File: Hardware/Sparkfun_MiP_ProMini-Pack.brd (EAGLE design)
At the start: 41.4 x 63.8 mm, 45 parts, among them Q1 8MHz, U1 ATMEGA328, U2 MIC5205, U3 TS3USB221A

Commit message: renamed files
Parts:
- added FID1, FID2: FIDUCIAL1X2, SparkFun-Aesthetics:FIDUCIAL-1X2
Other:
- board text added: "v10"
- board text removed: "v01"

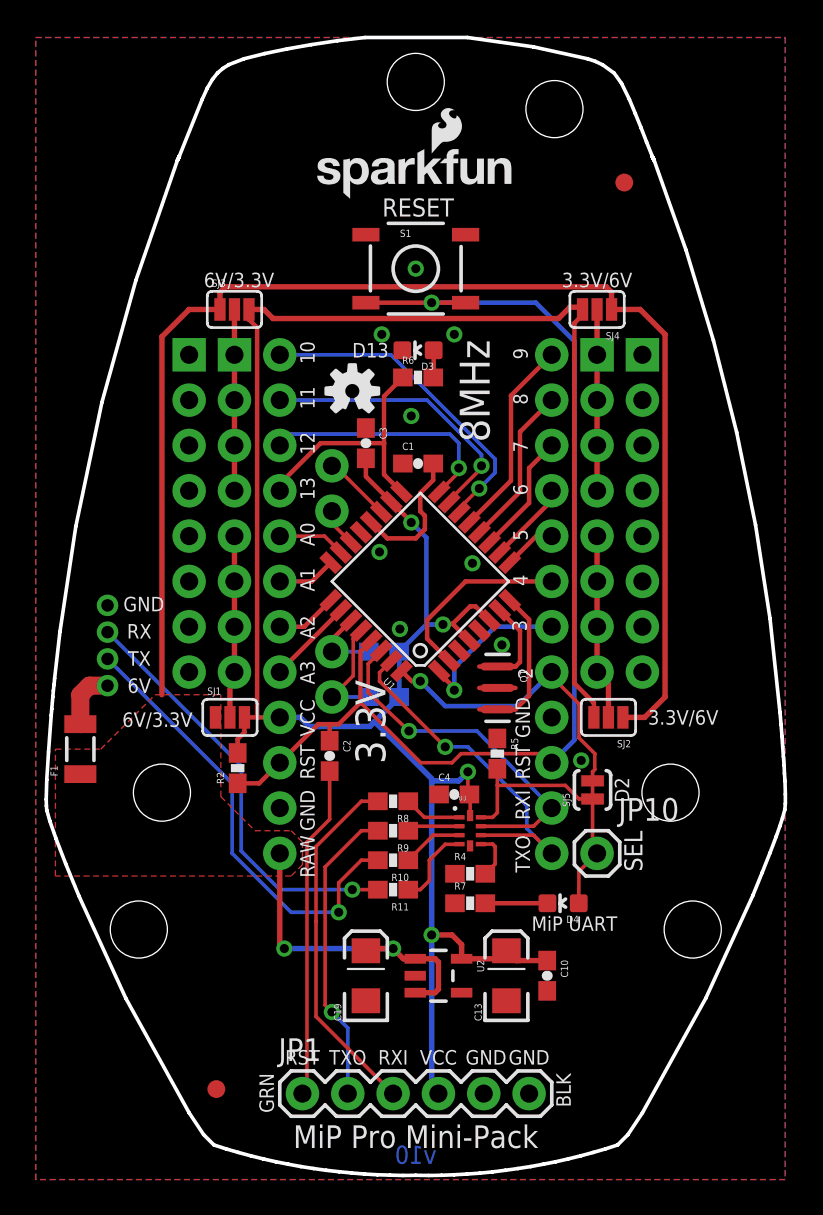
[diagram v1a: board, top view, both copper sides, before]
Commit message: added lables to servo pins to show pin modes
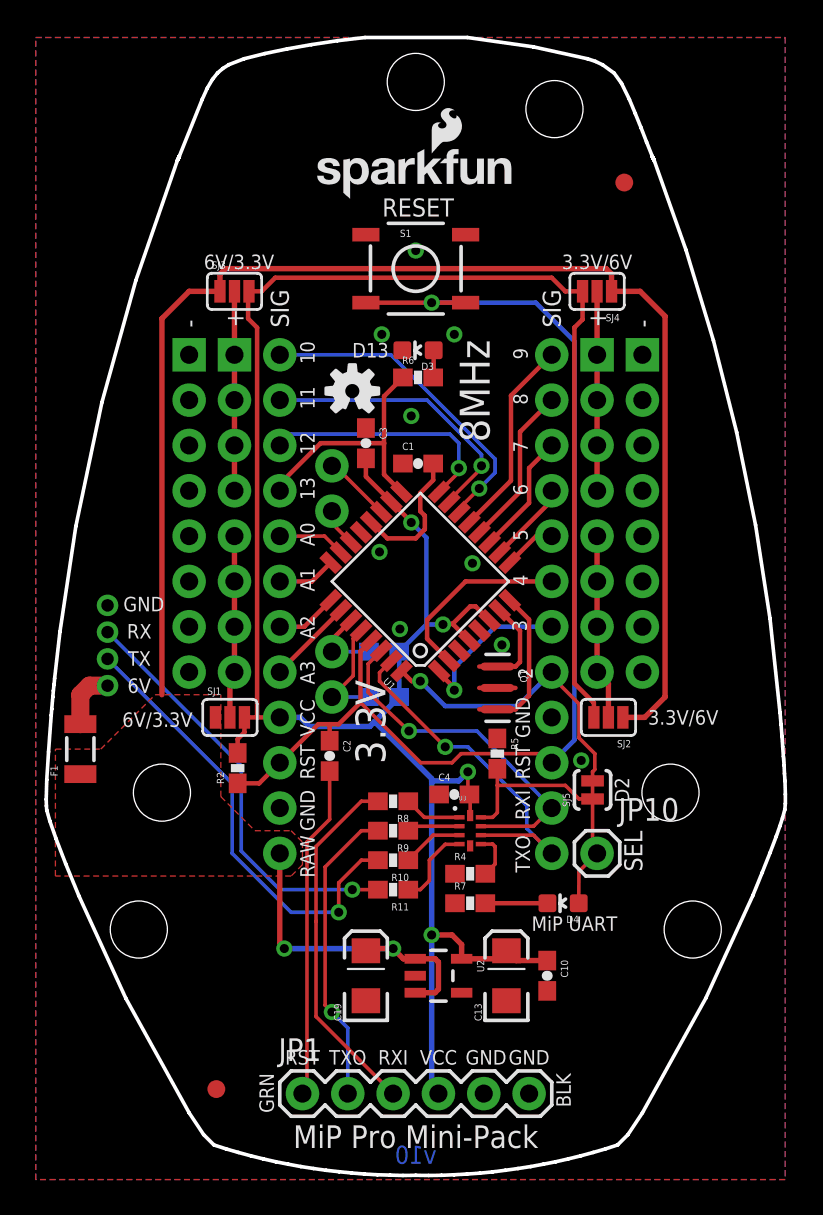
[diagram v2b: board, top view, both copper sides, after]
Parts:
- moved SJ3 1.02 mm to (11.2, 49.8)
- moved SJ4 1.02 mm to (31.5, 49.8)
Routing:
- net VCC: track 133.5 -> 135.7 mm
- net VIN: track 93.6 -> 95.7 mm
- net N$6: track 10.2 -> 11.2 mm
- net N$3: track 10.2 -> 11.2 mm
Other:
- board text added: "+"
- board text added: "-"
- board text added: "SIG"
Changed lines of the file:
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@@
 <setting verticaltext="up"/>
 </settings>
-<grid distance="0.1" unitdist="inch" unit="mil" style="lines" multiple="1" display="yes" altdistance="0.005" altunitdist="inch" altunit="inch"/>
+<grid distance="10" unitdist="mil" unit="mil" style="lines" multiple="1" display="yes" altdistance="0.005" altunitdist="inch" altunit="inch"/>
 <layers>
 <layer number="1" name="Top" color="4" fill="1" visible="yes" active="yes"/>
@@
 <text x="18.796" y="46.482" size="0.8128" layer="21" font="vector" ratio="15" rot="R180" align="center">D13</text>
 <text x="6.858" y="25.781" size="0.8128" layer="21" font="vector" ratio="15" align="center">6V/3.3V</text>
-<text x="11.43" y="50.419" size="0.8128" layer="21" font="vector" ratio="15" align="center">6V/3.3V</text>
-<text x="31.496" y="50.419" size="0.8128" layer="21" font="vector" ratio="15" align="center">3.3V/6V</text>
+<text x="11.43" y="51.435" size="0.8128" layer="21" font="vector" ratio="15" align="center">6V/3.3V</text>
+<text x="31.496" y="51.435" size="0.8128" layer="21" font="vector" ratio="15" align="center">3.3V/6V</text>
 <text x="36.322" y="25.908" size="0.8128" layer="21" font="vector" ratio="15" align="center">3.3V/6V</text>
 <text x="22.606" y="6.858" size="0.8128" layer="21" font="vector" ratio="15" align="center">VCC</text>
@@
 <text x="17.526" y="6.858" size="0.8128" layer="21" font="vector" ratio="15" align="center">TXO</text>
 <text x="14.986" y="6.858" size="0.8128" layer="21" font="vector" ratio="15" align="center">RST</text>
+<text x="13.716" y="47.752" size="1.016" layer="21" ratio="14" rot="R90" align="center-left">SIG</text>
+<text x="11.176" y="47.752" size="1.016" layer="21" ratio="14" rot="R90" align="center-left">+</text>
+<text x="8.636" y="47.752" size="1.016" layer="21" ratio="14" rot="R90" align="center-left">-</text>
+<text x="28.956" y="47.752" size="1.016" layer="21" ratio="14" rot="R90" align="center-left">SIG</text>
+<text x="31.496" y="47.752" size="1.016" layer="21" ratio="14" rot="R90" align="center-left">+</text>
+<text x="34.036" y="47.752" size="1.016" layer="21" ratio="14" rot="R90" align="center-left">-</text>
 </plain>
 <attributes>
@@
 <element name="JP9" library="SparkFun-Connectors" package="1X08" value="" x="11.176" y="46.228" rot="MR270"/>
 <element name="SJ2" library="SparkFun-Passives" package="PAD-JUMPER-3-2OF3_NC_BY_PASTE_YES_SILK_FULL_BOX" value="" x="32.131" y="25.908" rot="R180"/>
-<element name="SJ4" library="SparkFun-Passives" package="PAD-JUMPER-3-2OF3_NC_BY_PASTE_YES_SILK_FULL_BOX" value="" x="31.496" y="48.768" rot="R180"/>
+<element name="SJ4" library="SparkFun-Passives" package="PAD-JUMPER-3-2OF3_NC_BY_PASTE_YES_SILK_FULL_BOX" value="" x="31.496" y="49.784" rot="R180"/>
 <element name="U3" library="SparkFun-AnalogIC" package="QFN-10-RSE" value="TS3USB221A" x="24.384" y="19.558">
 <attribute name="PROD_ID" value="IC-12115" x="21.844" y="27.686" size="1.778" layer="27" display="off"/>
@@
 <element name="LOGO2" library="SparkFun-Aesthetics" package="OSHW-LOGO-S" value="OSHW-LOGOS" x="17.78" y="44.196"/>
 <element name="SJ1" library="SparkFun-Passives" package="PAD-JUMPER-3-2OF3_NC_BY_PASTE_YES_SILK_FULL_BOX" value="" x="10.922" y="25.908"/>
-<element name="SJ3" library="SparkFun-Passives" package="PAD-JUMPER-3-2OF3_NC_BY_PASTE_YES_SILK_FULL_BOX" value="" x="11.176" y="48.768"/>
+<element name="SJ3" library="SparkFun-Passives" package="PAD-JUMPER-3-2OF3_NC_BY_PASTE_YES_SILK_FULL_BOX" value="" x="11.176" y="49.784"/>
 <element name="C10" library="SparkFun" package="0603-CAP" value="0.1uF" x="28.702" y="11.43" rot="R270"/>
 <element name="C13" library="SparkFun" package="EIA3216" value="10uF" x="26.416" y="11.43" rot="R90"/>
@@
 <via x="26.162" y="29.972" extent="1-16" drill="0.508"/>
 <via x="19.431" y="47.371" extent="1-16" drill="0.508"/>
-<via x="21.336" y="51.054" extent="1-16" drill="0.508"/>
+<via x="21.336" y="52.07" extent="1-16" drill="0.508"/>
 <via x="23.495" y="47.371" extent="1-16" drill="0.508"/>
 <via x="21.082" y="42.799" extent="1-16" drill="0.508"/>
@@
 <wire x1="12.446" y1="25.908" x2="13.716" y2="25.908" width="0.254" layer="1"/>
 <wire x1="12.446" y1="47.752" x2="12.446" y2="25.908" width="0.254" layer="1"/>
-<wire x1="30.6832" y1="48.768" x2="30.6832" y2="48.4632" width="0.254" layer="1"/>
-<wire x1="30.6832" y1="48.4632" x2="30.226" y2="48.006" width="0.254" layer="1"/>
-<wire x1="11.9888" y1="48.2092" x2="12.446" y2="47.752" width="0.254" layer="1"/>
+<wire x1="30.6832" y1="49.784" x2="30.6832" y2="48.2092" width="0.254" layer="1"/>
+<wire x1="30.6832" y1="48.2092" x2="30.226" y2="47.752" width="0.254" layer="1"/>
+<wire x1="11.938" y1="48.26" x2="12.446" y2="47.752" width="0.254" layer="1"/>
 <contactref element="C4" pad="2"/>
 <wire x1="19.968884375" y1="37.9775375" x2="18.542" y2="39.404428125" width="0.254" layer="1"/>
@@
 <wire x1="24.257" y1="22.86" x2="23.749" y2="22.352" width="0.3048" layer="16"/>
 <wire x1="23.749" y1="22.352" x2="22.225" y2="22.352" width="0.3048" layer="16"/>
-<wire x1="30.5562" y1="48.895" x2="29.972" y2="48.895" width="0.3048" layer="1"/>
-<wire x1="29.972" y1="48.895" x2="29.337" y2="48.26" width="0.3048" layer="1"/>
-<wire x1="29.337" y1="48.26" x2="13.335" y2="48.26" width="0.3048" layer="1"/>
-<wire x1="13.335" y1="48.26" x2="12.827" y2="48.768" width="0.3048" layer="1"/>
-<wire x1="30.5562" y1="48.895" x2="30.6832" y2="48.768" width="0.3048" layer="1"/>
 <wire x1="22.606" y1="4.826" x2="22.225" y2="5.207" width="0.3048" layer="16"/>
 <wire x1="22.225" y1="5.207" x2="22.225" y2="13.716" width="0.3048" layer="16"/>
@@
 <contactref element="SJ3" pad="3"/>
 <wire x1="22.225" y1="13.716" x2="22.225" y2="22.352" width="0.3048" layer="16"/>
-<wire x1="11.9888" y1="48.768" x2="12.827" y2="48.768" width="0.3048" layer="1"/>
-<wire x1="11.9888" y1="48.2092" x2="11.9888" y2="48.768" width="0.3048" layer="1"/>
 <contactref element="C13" pad="A"/>
 <contactref element="C10" pad="1"/>
@@
 <wire x1="11.7348" y1="25.0698" x2="11.3538" y2="24.6888" width="0.254" layer="1"/>
 <wire x1="11.3538" y1="24.6888" x2="11.3538" y2="23.9132" width="0.254" layer="1"/>
-<wire x1="30.226" y1="48.006" x2="30.226" y2="27.813" width="0.254" layer="1"/>
+<wire x1="30.226" y1="47.752" x2="30.226" y2="27.813" width="0.254" layer="1"/>
 <wire x1="30.226" y1="27.813" x2="31.3182" y2="26.7208" width="0.254" layer="1"/>
 <wire x1="31.3182" y1="26.7208" x2="31.3182" y2="25.908" width="0.254" layer="1"/>
+<wire x1="11.9888" y1="49.784" x2="12.7" y2="49.784" width="0.254" layer="1"/>
+<wire x1="12.7" y1="49.784" x2="13.462" y2="50.546" width="0.254" layer="1"/>
+<wire x1="13.462" y1="50.546" x2="28.956" y2="50.546" width="0.254" layer="1"/>
+<wire x1="28.956" y1="50.546" x2="29.718" y2="49.784" width="0.254" layer="1"/>
+<wire x1="29.718" y1="49.784" x2="30.6832" y2="49.784" width="0.254" layer="1"/>
+<wire x1="11.938" y1="48.26" x2="11.938" y2="49.784" width="0.254" layer="1"/>
+<wire x1="11.9888" y1="49.784" x2="11.938" y2="49.784" width="0.254" layer="1"/>
 </signal>
 <signal name="D9">
@@
 <wire x1="11.176" y1="43.688" x2="11.176" y2="46.228" width="0.3048" layer="1"/>
 <contactref element="SJ3" pad="2"/>
-<wire x1="11.176" y1="48.768" x2="11.176" y2="46.228" width="0.3048" layer="1"/>
+<wire x1="11.176" y1="49.784" x2="11.176" y2="46.228" width="0.3048" layer="1"/>
 </signal>
 <signal name="N$6">
@@
 <contactref element="JP8" pad="4"/>
 <contactref element="SJ4" pad="2"/>
-<wire x1="31.496" y1="48.768" x2="31.496" y2="46.228" width="0.3048" layer="1"/>
+<wire x1="31.496" y1="49.784" x2="31.496" y2="46.228" width="0.3048" layer="1"/>
 <wire x1="31.496" y1="46.228" x2="31.496" y2="43.688" width="0.3048" layer="1"/>
 <wire x1="31.496" y1="43.688" x2="31.496" y2="41.148" width="0.3048" layer="1"/>
@@
 <contactref element="SJ2" pad="1"/>
 <contactref element="JP6" pad="1"/>
-<wire x1="32.3088" y1="48.768" x2="33.909" y2="48.768" width="0.3048" layer="1"/>
-<wire x1="33.909" y1="48.768" x2="35.306" y2="47.371" width="0.3048" layer="1"/>
-<wire x1="35.306" y1="47.371" x2="35.306" y2="27.051" width="0.3048" layer="1"/>
-<wire x1="32.3088" y1="49.7332" x2="32.004" y2="50.038" width="0.3048" layer="1"/>
-<wire x1="32.004" y1="50.038" x2="10.668" y2="50.038" width="0.3048" layer="1"/>
-<wire x1="10.668" y1="50.038" x2="10.3632" y2="49.7332" width="0.3048" layer="1"/>
-<wire x1="32.3088" y1="48.768" x2="32.3088" y2="49.7332" width="0.3048" layer="1"/>
+<wire x1="32.3088" y1="49.784" x2="33.909" y2="49.784" width="0.3048" layer="1"/>
+<wire x1="33.909" y1="49.784" x2="35.306" y2="48.387" width="0.3048" layer="1"/>
+<wire x1="35.306" y1="48.387" x2="35.306" y2="27.051" width="0.3048" layer="1"/>
+<wire x1="32.3088" y1="50.7492" x2="32.004" y2="51.054" width="0.3048" layer="1"/>
+<wire x1="32.004" y1="51.054" x2="10.668" y2="51.054" width="0.3048" layer="1"/>
+<wire x1="10.668" y1="51.054" x2="10.3632" y2="50.7492" width="0.3048" layer="1"/>
+<wire x1="32.3088" y1="49.784" x2="32.3088" y2="50.7492" width="0.3048" layer="1"/>
 <contactref element="F1" pad="1"/>
 <contactref element="SJ1" pad="1"/>
 <contactref element="SJ3" pad="1"/>
-<wire x1="10.3632" y1="49.7332" x2="10.3632" y2="48.768" width="0.3048" layer="1"/>
-<wire x1="7.112" y1="27.178" x2="7.112" y2="47.244" width="0.3048" layer="1"/>
-<wire x1="7.112" y1="47.244" x2="8.636" y2="48.768" width="0.3048" layer="1"/>
-<wire x1="8.636" y1="48.768" x2="10.3632" y2="48.768" width="0.3048" layer="1"/>
+<wire x1="10.3632" y1="50.7492" x2="10.3632" y2="49.784" width="0.3048" layer="1"/>
+<wire x1="7.112" y1="27.178" x2="7.112" y2="48.26" width="0.3048" layer="1"/>
+<wire x1="7.112" y1="48.26" x2="8.636" y2="49.784" width="0.3048" layer="1"/>
+<wire x1="8.636" y1="49.784" x2="10.3632" y2="49.784" width="0.3048" layer="1"/>
 <wire x1="35.306" y1="27.051" x2="34.163" y2="25.908" width="0.3048" layer="1"/>
 <wire x1="34.163" y1="25.908" x2="32.9438" y2="25.908" width="0.3048" layer="1"/>
@@
 </signal>
 </signals>
+<errors>
+</errors>
 </board>
 </drawing>

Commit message: addressing issues in github
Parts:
- R1, R3: value (none) -> DNP
- SJ5: value JUMPER-PAD-2-NC_BY_TRACE -> D2 Jumper
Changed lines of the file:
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@@
 <?xml version="1.0" encoding="utf-8"?>
 <!DOCTYPE eagle SYSTEM "eagle.dtd">
-<eagle version="6.5.0">
+<eagle version="6.6.0">
 <drawing>
 <settings>
@@
 <element name="JP1" library="SparkFun" package="1X06" value="FTDI Basic" x="14.986" y="4.826"/>
 <element name="C2" library="SparkFun" package="0603-CAP" value="0.1uF" x="16.51" y="23.749" rot="R270"/>
-<element name="R1" library="SparkFun" package="0603-RES" value="" x="19.558" y="29.591" rot="MR180"/>
-<element name="R3" library="SparkFun" package="0603-RES" value="" x="19.558" y="27.051" rot="MR180"/>
+<element name="R1" library="SparkFun" package="0603-RES" value="DNP" x="19.558" y="29.591" rot="MR180"/>
+<element name="R3" library="SparkFun" package="0603-RES" value="DNP" x="19.558" y="27.051" rot="MR180"/>
 <element name="S1" library="Testing" package="TACTILE-SWITCH-SMD-ALT01" value="Reset" x="21.336" y="51.054"/>
 <element name="JP3" library="SparkFun" package="1X02" value="" x="16.637" y="40.005" rot="MR270"/>
@@
 <element name="C4" library="SparkFun" package="0603-CAP" value="0.1uF" x="23.495" y="21.59"/>
 <element name="JP10" library="SparkFun-Connectors" package="1X01" value="M01PTH" x="31.496" y="18.288"/>
-<element name="SJ5" library="SparkFun-Passives" package="PAD-JUMPER-2-NC_BY_TRACE_YES_SILK" value="JUMPER-PAD-2-NC_BY_TRACE" x="31.242" y="21.844" rot="R90"/>
+<element name="SJ5" library="SparkFun-Passives" package="PAD-JUMPER-2-NC_BY_TRACE_YES_SILK" value="D2 Jumper" x="31.242" y="21.844" rot="R90"/>
 <element name="LOGO1" library="SparkFun-Aesthetics" package="SFE_LOGO_NAME_FLAME_.1" value="SFE_LOGO_NAME_FLAME.1_INCH" x="15.367" y="54.864"/>
 <element name="F1" library="SparkFun-PowerIC" package="PTC-1206" value="PTCSMD" x="2.54" y="24.13" rot="R90">
@@
 <signals>
 <signal name="GND">
-<polygon width="0.254" layer="16">
+<polygon width="0.254" layer="16" isolate="0.1524">
 <vertex x="42.037" y="64.008"/>
 <vertex x="42.037" y="0.008"/>
@@
 <vertex x="0.037" y="64.008"/>
 </polygon>
-<polygon width="0.254" layer="1" rank="6">
+<polygon width="0.254" layer="1" isolate="0.1524" rank="6">
 <vertex x="42.037" y="64.008"/>
 <vertex x="42.037" y="0.008"/>
@@
 <wire x1="22.418" y1="10.48" x2="22.606" y2="10.668" width="0.3048" layer="1"/>
 <wire x1="22.606" y1="10.668" x2="22.606" y2="12.192" width="0.3048" layer="1"/>
-<polygon width="0.3048" layer="1">
+<polygon width="0.3048" layer="1" isolate="0.3048">
 <vertex x="1.143" y="24.13"/>
 <vertex x="3.683" y="24.13"/>
